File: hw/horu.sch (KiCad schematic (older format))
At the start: 4 parts

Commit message: Schematic complete except for decoupling
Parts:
- removed C? (x2): 22 pF, symbol C_Small
- removed P?: CONN_01X30, symbol CONN_01X30
- removed Y?: Crystal_GND24, symbol Crystal_GND24
- added C101, C103, C104: 1.0 uF, symbol C_Small
- added C102, C105: 22 pF, symbol C_Small
- added C106: 2.2 uF, symbol C_Small
- added D101: GSOT05C-GS08, symbol D_Schottky_x2_ACom_KKA
- added D102, D103, D104, D105: LED_GREEN, symbol LED
- added J101: UX60SC-MB-5S8, MODULE, symbol UX60SC-MB-5S8
- added L101, L102: 330 Ohm, symbol L
- added P101: CONN_01X30, symbol CONN_01X30
- added P102: CONN_02X05, symbol CONN_02X05
- added R101, R102: 33, symbol R_Small
- added R103, R104, R105, R106: 220, symbol R_Small
- added R107: 0, symbol R_Small
- added TP101: TEST, symbol TEST
- added TP102, TP103, TP104, TP105, TP106, TP107, TP108, TP109, TP110, TP111: TEST_1P, symbol TEST_1P
- added U101: KL25P80M48SF0, 80 LQFN, symbol KL25P80M48SF0
- added Y101: 8MHz, symbol Crystal_GND24
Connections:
- net labels added: +3.3V, +3.3V_SDA, CON1, CON10, CON11, CON12, CON13, CON14, CON15, CON16, CON17, CON18, CON19, CON2, CON20, CON21, CON22, CON23, CON24, CON25, CON26, CON27, CON28, CON29, CON3, CON30, CON4, CON5, CON6, CON7, CON8, CON9, CON[30:1], DBG0, DBG1, DBG2, DBG3, LED0, LED1, LED2, LED3, RESETn, SWD_CLK, SWD_DIO, UART_RX, UART_TX, USB_DN, USB_DP, USB_ID, VUSB
- wire segments 11 -> 165
- no-connect marks 0 -> 21
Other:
- note added: "CAD NOTE:\nPlease place these capacitors\nnear their respective CPU pin\n(VREFH to VREFL\nand VDDA to VSSA)"

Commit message: Define some footprints
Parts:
- C101, C102, C103, C104, C105, C106, L101, L102, R101, R102, R103, R104, R105, R106: footprint (none) -> Resistors_SMD:R_0603_HandSoldering
- D101: footprint (none) -> TO_SOT_Packages_SMD:SOT-23_Handsoldering
- D102, D103, D104, D105: footprint (none) -> LEDs:LED_0603
- P102: footprint (none) -> Pin_Headers:Pin_Header_Straight_2x05_Pitch1.27mm_SMD
- R107: footprint (none) -> Resistors_SMD:R_0402
- TP101, TP102, TP103, TP104, TP105, TP106, TP107, TP108, TP109, TP110, TP111: footprint (none) -> Measurement_Points:Measurement_Point_Round-TH_Small
- U101: footprint 80 LQFN -> Housings_QFP:LQFP-80_12x12mm_Pitch0.5mm
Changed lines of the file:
@@
 F 0 "C105" H 5360 5070 50  0000 L CNN
 F 1 "22 pF" H 5360 4920 50  0000 L CNN
-F 2 "" H 5350 5000 50  0001 C CNN
+F 2 "Resistors_SMD:R_0603_HandSoldering" H 5350 5000 50  0001 C CNN
 F 3 "" H 5350 5000 50  0000 C CNN
 	1    5350 5000
@@
 F 0 "C102" H 4460 5070 50  0000 L CNN
 F 1 "22 pF" H 4460 4920 50  0000 L CNN
-F 2 "" H 4450 5000 50  0001 C CNN
+F 2 "Resistors_SMD:R_0603_HandSoldering" H 4450 5000 50  0001 C CNN
 F 3 "" H 4450 5000 50  0000 C CNN
 	1    4450 5000
@@
 F 0 "L101" V 1250 3700 50  0000 C CNN
 F 1 "330 Ohm" V 1375 3700 50  0000 C CNN
-F 2 "" H 1300 3700 50  0001 C CNN
+F 2 "Resistors_SMD:R_0603_HandSoldering" H 1300 3700 50  0001 C CNN
 F 3 "" H 1300 3700 50  0000 C CNN
 	1    1300 3700
@@
 F 0 "TP101" V 2025 3000 50  0000 C BNN
 F 1 "TEST" H 2000 2950 50  0001 C CNN
-F 2 "" H 2000 2700 50  0001 C CNN
+F 2 "Measurement_Points:Measurement_Point_Round-TH_Small" H 2000 2700 50  0001 C CNN
 F 3 "" H 2000 2700 50  0000 C CNN
 	1    2000 2700
@@
 F 0 "L102" V 2000 2050 50  0000 C CNN
 F 1 "330 Ohm" V 2125 2050 50  0000 C CNN
-F 2 "" H 2050 2050 50  0001 C CNN
+F 2 "Resistors_SMD:R_0603_HandSoldering" H 2050 2050 50  0001 C CNN
 F 3 "" H 2050 2050 50  0000 C CNN
 	1    2050 2050
@@
 F 0 "C101" H 2760 2370 50  0000 L CNN
 F 1 "1.0 uF" H 2760 2220 50  0000 L CNN
-F 2 "" H 2750 2300 50  0001 C CNN
+F 2 "Resistors_SMD:R_0603_HandSoldering" H 2750 2300 50  0001 C CNN
 F 3 "" H 2750 2300 50  0000 C CNN
 	1    2750 2300
@@
 F 0 "R101" V 2500 2500 50  0000 L CNN
 F 1 "33" V 2500 2900 50  0000 L CNN
-F 2 "" H 2550 2800 50  0001 C CNN
+F 2 "Resistors_SMD:R_0603_HandSoldering" H 2550 2800 50  0001 C CNN
 F 3 "" H 2550 2800 50  0000 C CNN
 	1    2550 2800
@@
 F 0 "R102" V 2500 2600 50  0000 L CNN
 F 1 "33" V 2500 3000 50  0000 L CNN
-F 2 "" H 2550 2900 50  0001 C CNN
+F 2 "Resistors_SMD:R_0603_HandSoldering" H 2550 2900 50  0001 C CNN
 F 3 "" H 2550 2900 50  0000 C CNN
 	1    2550 2900
@@
 F 0 "D101" H 2300 3350 50  0000 C CNN
 F 1 "GSOT05C-GS08" H 2250 3550 50  0000 C CNN
-F 2 "" H 2250 3450 50  0001 C CNN
+F 2 "TO_SOT_Packages_SMD:SOT-23_Handsoldering" H 2250 3450 50  0001 C CNN
 F 3 "" H 2250 3450 50  0000 C CNN
 	1    2250 3450
@@
 F 0 "U101" H 4650 3450 50  0000 C CNN
 F 1 "KL25P80M48SF0" H 4900 3350 50  0000 C CNN
-F 2 "80 LQFN" H 5050 3450 50  0001 C CNN
+F 2 "Housings_QFP:LQFP-80_12x12mm_Pitch0.5mm" H 5050 3450 50  0001 C CNN
 F 3 "KL25P80M48SF0-782763.pdf" H 5150 3550 50  0001 C CNN
 	2    4600 3300
@@
 F 0 "C106" H 5660 3920 50  0000 L CNN
 F 1 "2.2 uF" H 5660 3770 50  0000 L CNN
-F 2 "" H 5650 3850 50  0001 C CNN
+F 2 "Resistors_SMD:R_0603_HandSoldering" H 5650 3850 50  0001 C CNN
 F 3 "" H 5650 3850 50  0000 C CNN
 	1    5650 3850
@@
 F 0 "R107" V 5700 3400 50  0000 L CNN
 F 1 "0" V 5700 3150 50  0000 L CNN
-F 2 "" H 5650 3300 50  0001 C CNN
+F 2 "Resistors_SMD:R_0402" H 5650 3300 50  0001 C CNN
 F 3 "" H 5650 3300 50  0000 C CNN
 	1    5650 3300
@@
 F 0 "U101" H 4750 1050 50  0000 C CNN
 F 1 "KL25P80M48SF0" H 4950 950 50  0000 C CNN
-F 2 "80 LQFN" H 5100 1050 50  0001 C CNN
+F 2 "Housings_QFP:LQFP-80_12x12mm_Pitch0.5mm" H 5100 1050 50  0001 C CNN
 F 3 "KL25P80M48SF0-782763.pdf" H 5200 1150 50  0001 C CNN
 	1    4650 900
@@
 F 0 "C103" V 4900 1550 50  0000 L CNN
 F 1 "1.0 uF" V 4900 1900 50  0000 L CNN
-F 2 "" H 4950 1800 50  0001 C CNN
+F 2 "Resistors_SMD:R_0603_HandSoldering" H 4950 1800 50  0001 C CNN
 F 3 "" H 4950 1800 50  0000 C CNN
 	1    4950 1800
@@
 F 0 "C104" V 4900 1700 50  0000 L CNN
 F 1 "1.0 uF" V 4900 2050 50  0000 L CNN
-F 2 "" H 4950 1950 50  0001 C CNN
+F 2 "Resistors_SMD:R_0603_HandSoldering" H 4950 1950 50  0001 C CNN
 F 3 "" H 4950 1950 50  0000 C CNN
 	1    4950 1950
@@
 F 0 "U101" H 7500 3600 50  0000 C CNN
 F 1 "KL25P80M48SF0" H 7750 3500 50  0000 C CNN
-F 2 "80 LQFN" H 7900 3600 50  0001 C CNN
+F 2 "Housings_QFP:LQFP-80_12x12mm_Pitch0.5mm" H 7900 3600 50  0001 C CNN
 F 3 "KL25P80M48SF0-782763.pdf" H 8000 3700 50  0001 C CNN
 	4    7450 3450
@@
 F 0 "P102" H 2500 6800 50  0000 C CNN
 F 1 "CONN_02X05" H 2500 6200 50  0000 C CNN
-F 2 "" H 2500 5300 50  0001 C CNN
+F 2 "Pin_Headers:Pin_Header_Straight_2x05_Pitch1.27mm_SMD" H 2500 5300 50  0001 C CNN
 F 3 "" H 2500 5300 50  0000 C CNN
 	1    2500 6500
@@
 F 0 "D102" V 2800 5000 50  0000 C CNN
 F 1 "LED_GREEN" V 2700 4850 50  0001 C CNN
-F 2 "" H 2700 5100 50  0001 C CNN
+F 2 "LEDs:LED_0603" H 2700 5100 50  0001 C CNN
 F 3 "" H 2700 5100 50  0000 C CNN
 	1    2700 5100
@@
 F 0 "R103" H 2450 4700 50  0000 L CNN
 F 1 "220" H 2500 4800 50  0000 L CNN
-F 2 "" H 2700 4750 50  0001 C CNN
+F 2 "Resistors_SMD:R_0603_HandSoldering" H 2700 4750 50  0001 C CNN
 F 3 "" H 2700 4750 50  0000 C CNN
 	1    2700 4750
@@
 F 0 "TP102" V 6900 1350 50  0000 C CNN
 F 1 "TEST_1P" V 6800 1350 50  0001 C CNN
-F 2 "" H 7100 1050 50  0001 C CNN
+F 2 "Measurement_Points:Measurement_Point_Round-TH_Small" H 7100 1050 50  0001 C CNN
 F 3 "" H 7100 1050 50  0000 C CNN
 	1    6900 1050
@@
 F 0 "TP103" V 6900 1550 50  0000 C CNN
 F 1 "TEST_1P" V 6800 1550 50  0001 C CNN
-F 2 "" H 7100 1250 50  0001 C CNN
+F 2 "Measurement_Points:Measurement_Point_Round-TH_Small" H 7100 1250 50  0001 C CNN
 F 3 "" H 7100 1250 50  0000 C CNN
 	1    6900 1250
@@
 F 0 "U101" H 4200 6550 50  0000 C CNN
 F 1 "KL25P80M48SF0" H 4450 6450 50  0000 C CNN
-F 2 "80 LQFN" H 4600 6550 50  0001 C CNN
+F 2 "Housings_QFP:LQFP-80_12x12mm_Pitch0.5mm" H 4600 6550 50  0001 C CNN
 F 3 "KL25P80M48SF0-782763.pdf" H 4700 6650 50  0001 C CNN
 	5    4150 6400
@@
 F 0 "U101" H 7550 900 50  0000 C CNN
 F 1 "KL25P80M48SF0" H 7800 800 50  0000 C CNN
-F 2 "80 LQFN" H 7950 900 50  0001 C CNN
+F 2 "Housings_QFP:LQFP-80_12x12mm_Pitch0.5mm" H 7950 900 50  0001 C CNN
 F 3 "KL25P80M48SF0-782763.pdf" H 8050 1000 50  0001 C CNN
 	3    7500 750
@@
 F 0 "TP108" V 6900 2350 50  0000 C CNN
 F 1 "TEST_1P" V 6800 2350 50  0001 C CNN
-F 2 "" H 7100 2050 50  0001 C CNN
+F 2 "Measurement_Points:Measurement_Point_Round-TH_Small" H 7100 2050 50  0001 C CNN
 F 3 "" H 7100 2050 50  0000 C CNN
 	1    6900 2050
@@
 F 0 "TP104" V 6900 1950 50  0000 C CNN
 F 1 "TEST_1P" V 6800 1950 50  0001 C CNN
-F 2 "" H 7100 1650 50  0001 C CNN
+F 2 "Measurement_Points:Measurement_Point_Round-TH_Small" H 7100 1650 50  0001 C CNN
 F 3 "" H 7100 1650 50  0000 C CNN
 	1    6900 1650
@@
 F 0 "TP105" V 6900 2050 50  0000 C CNN
 F 1 "TEST_1P" V 6800 2050 50  0001 C CNN
-F 2 "" H 7100 1750 50  0001 C CNN
+F 2 "Measurement_Points:Measurement_Point_Round-TH_Small" H 7100 1750 50  0001 C CNN
 F 3 "" H 7100 1750 50  0000 C CNN
 	1    6900 1750
@@
 F 0 "TP106" V 6900 2150 50  0000 C CNN
 F 1 "TEST_1P" V 6800 2150 50  0001 C CNN
-F 2 "" H 7100 1850 50  0001 C CNN
+F 2 "Measurement_Points:Measurement_Point_Round-TH_Small" H 7100 1850 50  0001 C CNN
 F 3 "" H 7100 1850 50  0000 C CNN
 	1    6900 1850
@@
 F 0 "TP107" V 6900 2250 50  0000 C CNN
 F 1 "TEST_1P" V 6800 2250 50  0001 C CNN
-F 2 "" H 7100 1950 50  0001 C CNN
+F 2 "Measurement_Points:Measurement_Point_Round-TH_Small" H 7100 1950 50  0001 C CNN
 F 3 "" H 7100 1950 50  0000 C CNN
 	1    6900 1950
@@
 F 0 "TP109" V 6900 2550 50  0000 C CNN
 F 1 "TEST_1P" V 6800 2550 50  0001 C CNN
-F 2 "" H 7100 2250 50  0001 C CNN
+F 2 "Measurement_Points:Measurement_Point_Round-TH_Small" H 7100 2250 50  0001 C CNN
 F 3 "" H 7100 2250 50  0000 C CNN
 	1    6900 2250
@@
 F 0 "TP110" V 6900 2750 50  0000 C CNN
 F 1 "TEST_1P" V 6800 2750 50  0001 C CNN
-F 2 "" H 7100 2450 50  0001 C CNN
+F 2 "Measurement_Points:Measurement_Point_Round-TH_Small" H 7100 2450 50  0001 C CNN
 F 3 "" H 7100 2450 50  0000 C CNN
 	1    6900 2450
@@
 F 0 "TP111" V 6900 2850 50  0000 C CNN
 F 1 "TEST_1P" V 6800 2850 50  0001 C CNN
-F 2 "" H 7100 2550 50  0001 C CNN
+F 2 "Measurement_Points:Measurement_Point_Round-TH_Small" H 7100 2550 50  0001 C CNN
 F 3 "" H 7100 2550 50  0000 C CNN
 	1    6900 2550
@@
 F 0 "D103" V 3100 5000 50  0000 C CNN
 F 1 "LED_GREEN" V 3000 4850 50  0001 C CNN
-F 2 "" H 3000 5100 50  0001 C CNN
+F 2 "LEDs:LED_0603" H 3000 5100 50  0001 C CNN
 F 3 "" H 3000 5100 50  0000 C CNN
 	1    3000 5100
@@
 F 0 "R104" H 2750 4700 50  0000 L CNN
 F 1 "220" H 2800 4800 50  0000 L CNN
-F 2 "" H 3000 4750 50  0001 C CNN
+F 2 "Resistors_SMD:R_0603_HandSoldering" H 3000 4750 50  0001 C CNN
 F 3 "" H 3000 4750 50  0000 C CNN
 	1    3000 4750
@@
 F 0 "D104" V 3400 5000 50  0000 C CNN
 F 1 "LED_GREEN" V 3300 4850 50  0001 C CNN
-F 2 "" H 3300 5100 50  0001 C CNN
+F 2 "LEDs:LED_0603" H 3300 5100 50  0001 C CNN
 F 3 "" H 3300 5100 50  0000 C CNN
 	1    3300 5100
@@
 F 0 "R105" H 3050 4700 50  0000 L CNN
 F 1 "220" H 3100 4800 50  0000 L CNN
-F 2 "" H 3300 4750 50  0001 C CNN
+F 2 "Resistors_SMD:R_0603_HandSoldering" H 3300 4750 50  0001 C CNN
 F 3 "" H 3300 4750 50  0000 C CNN
 	1    3300 4750
@@
 F 0 "D105" V 3700 5000 50  0000 C CNN
 F 1 "LED_GREEN" V 3600 4850 50  0001 C CNN
-F 2 "" H 3600 5100 50  0001 C CNN
+F 2 "LEDs:LED_0603" H 3600 5100 50  0001 C CNN
 F 3 "" H 3600 5100 50  0000 C CNN
 	1    3600 5100
@@
 F 0 "R106" H 3350 4700 50  0000 L CNN
 F 1 "220" H 3400 4800 50  0000 L CNN
-F 2 "" H 3600 4750 50  0001 C CNN
+F 2 "Resistors_SMD:R_0603_HandSoldering" H 3600 4750 50  0001 C CNN
 F 3 "" H 3600 4750 50  0000 C CNN
 	1    3600 4750

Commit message: Drop opensda circuit
This makes room in BOM for fancy USB switch letting either USB-C port be connected to PC, while other can connect (in future) to keypad
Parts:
- removed C101: 1.0 uF, Resistors_SMD:R_0603_HandSoldering, symbol C_Small
- removed D101: GSOT05C-GS08, TO_SOT_Packages_SMD:SOT-23_Handsoldering, symbol D_Schottky_x2_ACom_KKA
- removed J101: UX60SC-MB-5S8, MODULE, symbol UX60SC-MB-5S8
- removed L101, L102: 330 Ohm, Resistors_SMD:R_0603_HandSoldering, symbol L
- removed R101, R102: 33, Resistors_SMD:R_0603_HandSoldering, symbol R_Small
- removed TP101: TEST, Measurement_Points:Measurement_Point_Round-TH_Small, symbol TEST
- added R105, R106: 33, Resistors_SMD:R_0603_HandSoldering, symbol R_Small
- renumbered C102 to C101, C103 to C102, C104 to C103, C105 to C104, C106 to C105, D102 to D101, D103 to D102, D104 to D103, D105 to D104, R103 to R101, R104 to R102, R105 to R103, R106 to R104, TP102 to TP101, TP103 to TP102, TP104 to TP103, TP105 to TP104, TP106 to TP105, TP107 to TP106, TP108 to TP107, TP109 to TP108, TP110 to TP109, TP111 to TP110
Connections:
- net labels added: UART_SEL, USB_OEn, USB_SEL, USB_SENSE_A
- net labels removed: +3.3V_SDA, USB_ID
- wire segments 165 -> 143
- no-connect marks 21 -> 17

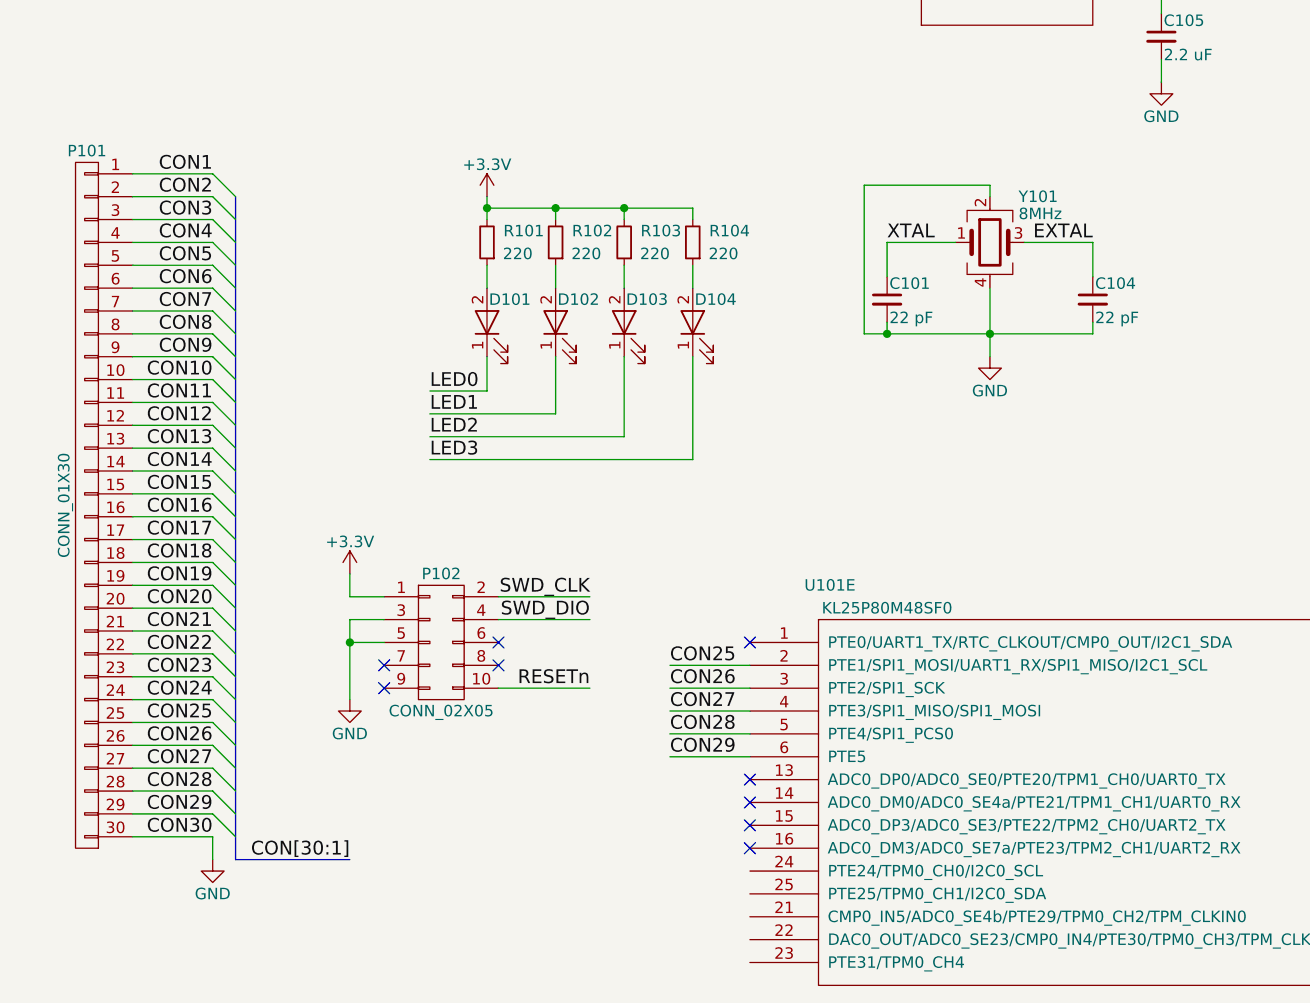
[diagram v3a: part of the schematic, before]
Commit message: Add some more footprints
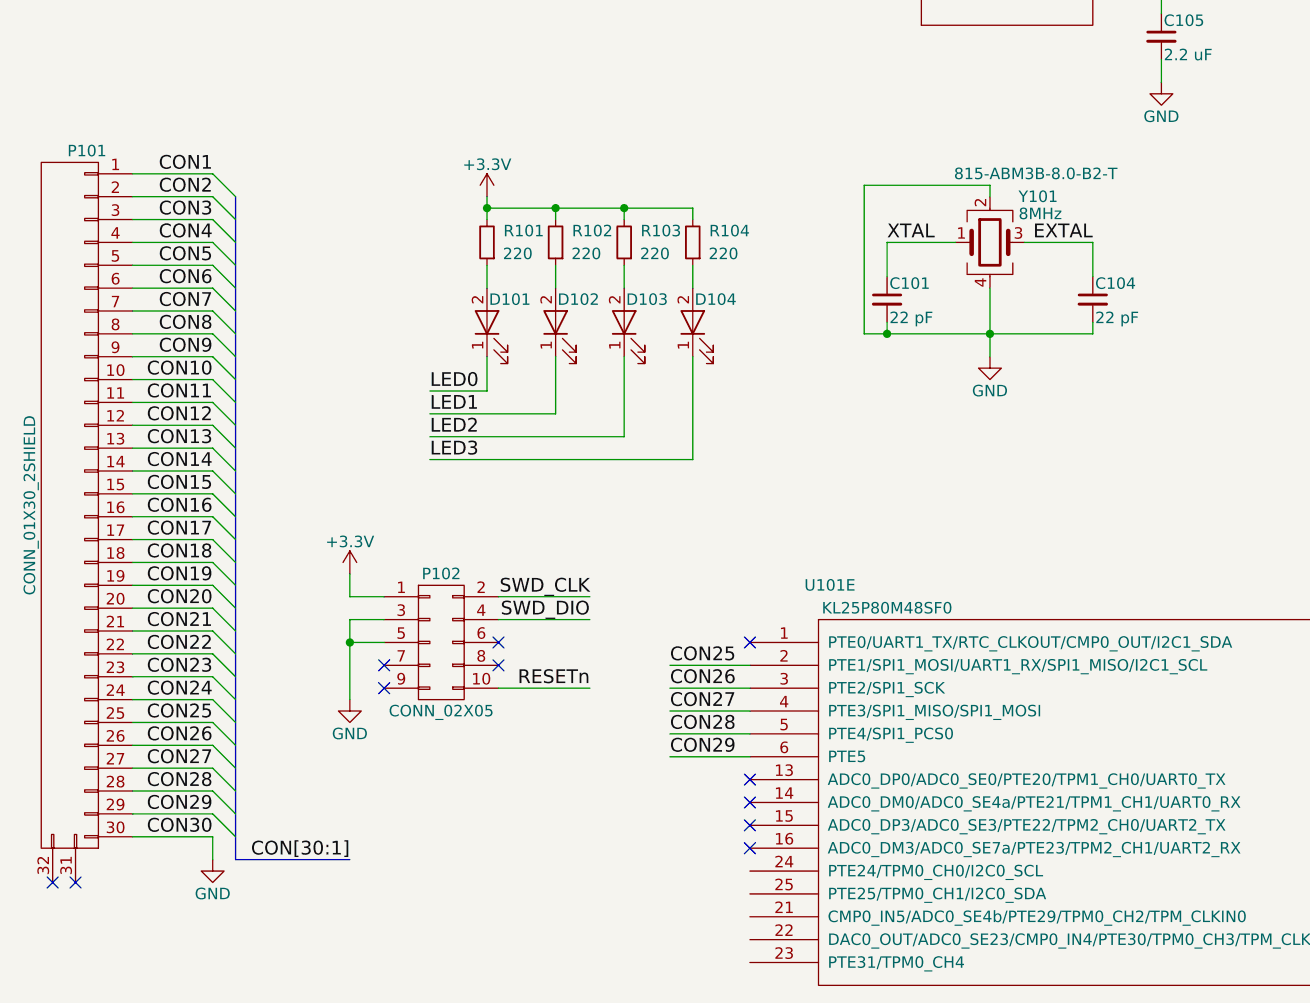
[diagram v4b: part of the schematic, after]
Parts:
- removed P101: CONN_01X30, symbol CONN_01X30
- added P101: CONN_01X30_2SHIELD, horu:52271-3079, symbol CONN_01X30_2SHIELD
- Y101: footprint (none) -> Crystals:Crystal_SMD_Abracon_ABM3B-4pin_5.0x3.2mm
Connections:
- net CON1: now also P101.1 (P1)
- net CON10: now also P101.10 (P10)
- net CON11: now also P101.11 (P11)
- net CON12: now also P101.12 (P12)
- net CON13: now also P101.13 (P13)
- net CON14: now also P101.14 (P14)
- net CON15: now also P101.15 (P15)
- net CON16: now also P101.16 (P16)
- net CON17: now also P101.17 (P17)
- net CON18: now also P101.18 (P18)
- net CON19: now also P101.19 (P19)
- net CON2: now also P101.2 (P2)
- net CON20: now also P101.20 (P20)
- net CON21: now also P101.21 (P21)
- net CON22: now also P101.22 (P22)
- net CON23: now also P101.23 (P23)
- net CON24: now also P101.24 (P24)
- net CON25: now also P101.25 (P25)
- net CON26: now also P101.26 (P26)
- net CON27: now also P101.27 (P27)
- net CON28: now also P101.28 (P28)
- net CON29: now also P101.29 (P29)
- net CON3: now also P101.3 (P3)
- net CON4: now also P101.4 (P4)
- net CON5: now also P101.5 (P5)
- net CON6: now also P101.6 (P6)
- net CON7: now also P101.7 (P7)
- net CON8: now also P101.8 (P8)
- net CON9: now also P101.9 (P9)
- net GND: now also P101.30 (P30)
- no-connect marks 17 -> 19
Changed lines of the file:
@@
 F 0 "Y101" H 5025 4950 50  0000 L CNN
 F 1 "8MHz" H 5025 4875 50  0000 L CNN
-F 2 "" H 4900 4750 50  0001 C CNN
-F 3 "" H 4900 4750 50  0000 C CNN
+F 2 "Crystals:Crystal_SMD_Abracon_ABM3B-4pin_5.0x3.2mm" H 4900 4750 50  0001 C CNN
+F 3 "815-ABM3B-8.0-B2-T" H 5100 5050 50  0000 C CNN
 	1    4900 4750
 	1    0    0    -1
@@
 	1    4900 5250
 	1    0    0    -1
-$EndComp
-$Comp
-L CONN_01X30 P101
-U 1 1 589874B6
-P 950 5900
-F 0 "P101" H 950 7450 50  0000 C CNN
-F 1 "CONN_01X30" V 1050 5900 50  0000 C CNN
-F 2 "" H 950 5900 50  0001 C CNN
-F 3 "" H 950 5900 50  0000 C CNN
-	1    950  5900
-	-1   0    0    -1
 $EndComp
 Text Label 2100 7450 2    60   ~ 0
@@
 	1    0    0    -1
 $EndComp
+$Comp
+L CONN_01X30_2SHIELD P101
+U 1 1 589DDD38
+P 950 5900
+F 0 "P101" H 950 7450 50  0000 C CNN
+F 1 "CONN_01X30_2SHIELD" V 1200 5900 50  0000 C CNN
+F 2 "horu:52271-3079" H 950 5900 50  0001 C CNN
+F 3 "" H 950 5900 50  0000 C CNN
+	1    950  5900
+	-1   0    0    -1
+$EndComp
+NoConn ~ 800  7550
+NoConn ~ 900  7550
 $EndSCHEMATC
